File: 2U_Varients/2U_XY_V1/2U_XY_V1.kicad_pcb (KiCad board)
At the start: 4 copper layers, 83 x 212.6 mm, 31 parts, among them CN1 DF11-2DSA-4DP, J112 Conn_01x01, J114 Conn_01x01, J12 Conn_01x01, J14 Conn_01x01, J2 Conn_01x01, J3 Conn_01x01, J4 Conn_01x01, J5 Conn_01x01, U2 TMP112xxDRL, U3 DRV2605LDGS, U4 TCA4311ADGKR, U5 5040500691, U7 VEML6031X00

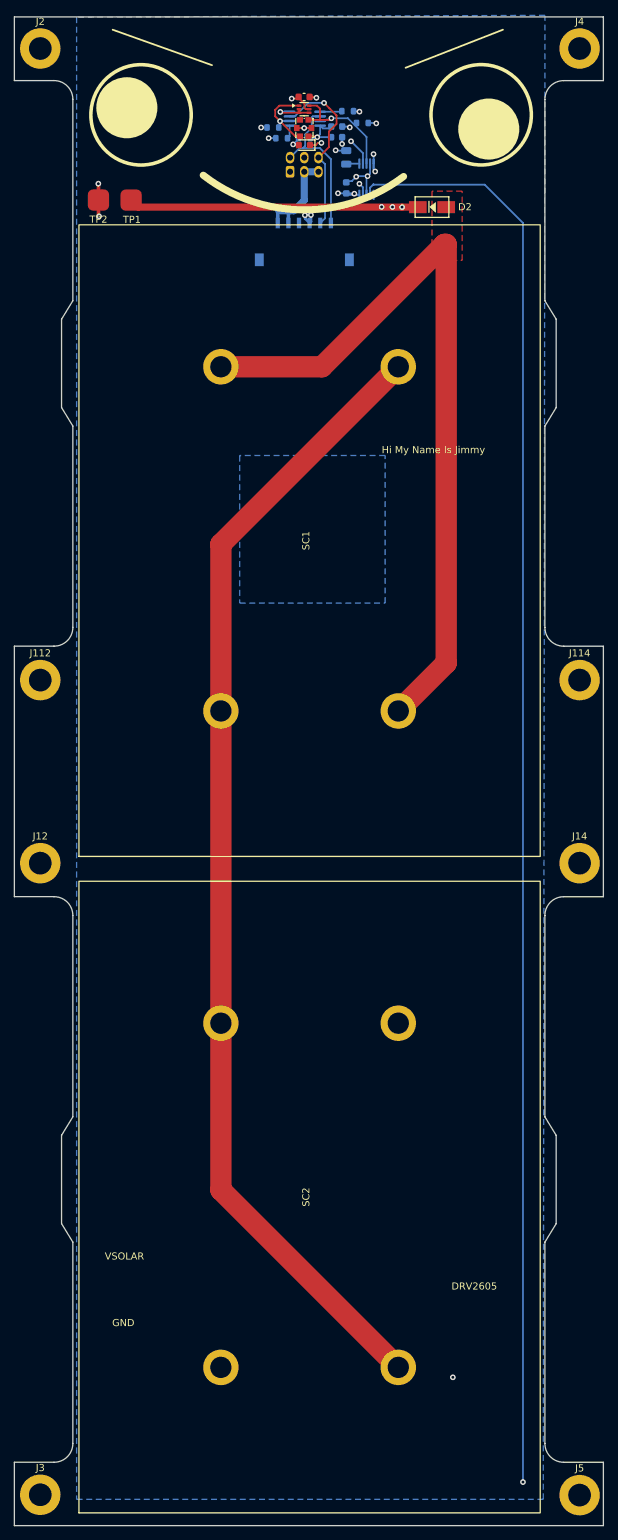
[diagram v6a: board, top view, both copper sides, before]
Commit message: Fixed Solar Cell Polarity
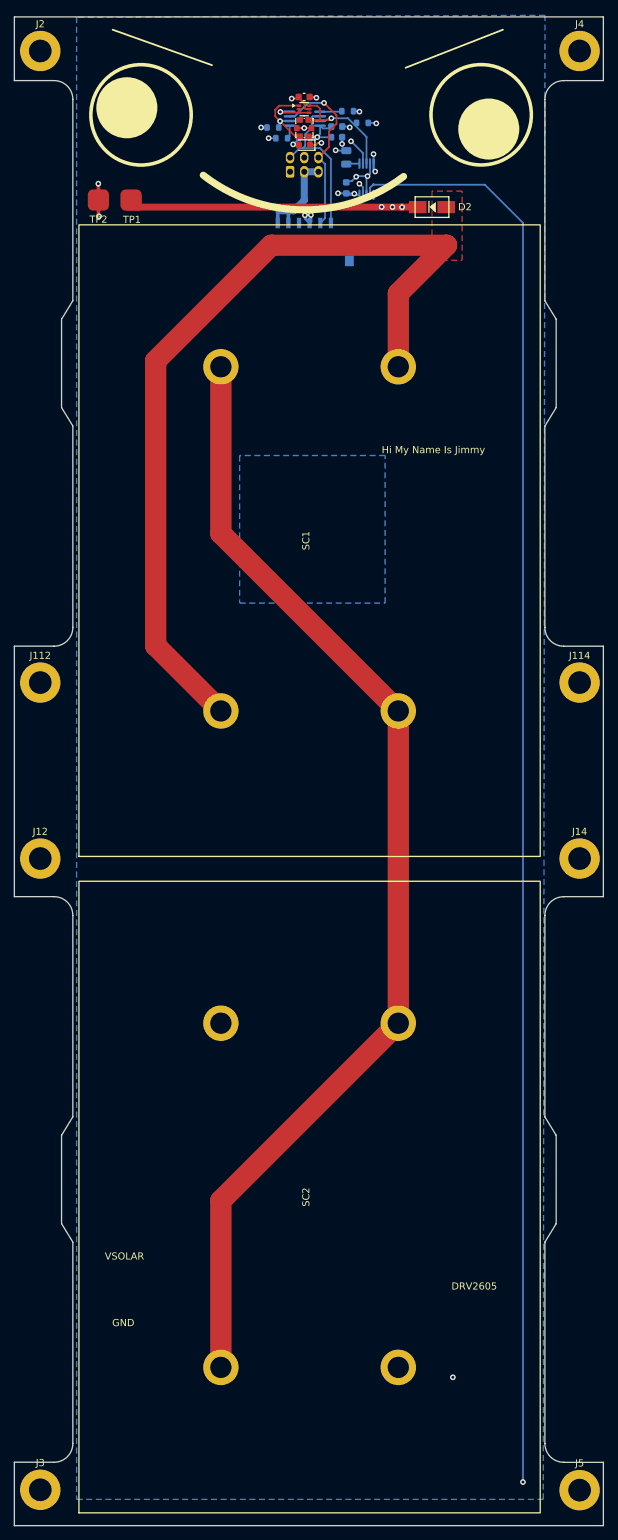
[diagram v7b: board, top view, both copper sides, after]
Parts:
- moved J3 0.70 mm to (171.8, 243.8)
- moved J5 0.70 mm to (247.8, 243.8)
- moved J12 0.65 mm to (171.8, 154.8)
- moved J14 0.65 mm to (247.8, 154.8)
- moved J2 0.35 mm to (171.8, 41.0)
- moved J4 0.35 mm to (247.8, 41.0)
- moved J112 0.35 mm to (171.8, 130.0)
- moved J114 0.35 mm to (247.8, 130.0)
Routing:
- net /SOL_OUT: track 107.4 -> 120.8 mm
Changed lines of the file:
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@@
 	(footprint "MountingHole:MountingHole_3.2mm_M3_ISO7380_Pad"
 		(layer "F.Cu")
-		(at 171.800001 40.65)
+		(at 171.800001 41)
 		(descr "Mounting Hole 3.2mm, M3, generated by kicad-footprint-generator mountinghole.py")
 		(tags "mountinghole M3 ISO7380")
@@
 	(footprint "MountingHole:MountingHole_3.2mm_M3_ISO7380_Pad"
 		(layer "F.Cu")
-		(at 247.800001 40.65)
+		(at 247.800001 41)
 		(descr "Mounting Hole 3.2mm, M3, generated by kicad-footprint-generator mountinghole.py")
 		(tags "mountinghole M3 ISO7380")
@@
 	(footprint "MountingHole:MountingHole_3.2mm_M3_ISO7380_Pad"
 		(layer "F.Cu")
-		(at 171.800001 244.45)
+		(at 171.800001 243.75)
 		(descr "Mounting Hole 3.2mm, M3, generated by kicad-footprint-generator mountinghole.py")
 		(tags "mountinghole M3 ISO7380")
@@
 			(layer "Dwgs.User")
 			(pts
-				(xy 177.25 85.5) (xy 197.25 85)
+				(xy 177.25 65.5) (xy 177.25 85.5)
 			)
-			(height 5.5)
-			(orientation 0)
+			(height -7)
+			(orientation 1)
 			(format
 				(prefix "")
@@
 			)
 			(gr_text "20"
-				(at 187.25 89.85 0)
+				(at 169.1 75.5 90)
 				(layer "Dwgs.User")
 				(effects
@@
 			(layer "Dwgs.User")
 			(pts
-				(xy 177.25 134.5) (xy 197.25 134.5)
+				(xy 177.25 154.5) (xy 177.25 134.5)
 			)
-			(height -4.5)
-			(orientation 0)
+			(height -2.5)
+			(orientation 1)
 			(format
 				(prefix "")
@@
 			)
 			(gr_text "20"
-				(at 187.25 128.85 0)
+				(at 173.6 144.5 90)
 				(layer "Dwgs.User")
 				(effects
@@
 			(layer "Dwgs.User")
 			(pts
-				(xy 177.25 65.5) (xy 177.25 85.5)
+				(xy 177.25 85.5) (xy 197.25 85)
 			)
-			(height -7)
-			(orientation 1)
+			(height 5.5)
+			(orientation 0)
 			(format
 				(prefix "")
@@
 			)
 			(gr_text "20"
-				(at 169.1 75.5 90)
+				(at 187.25 89.85 0)
 				(layer "Dwgs.User")
 				(effects
@@
 			(layer "Dwgs.User")
 			(pts
-				(xy 177.25 154.5) (xy 177.25 134.5)
+				(xy 242.25 65.5) (xy 222.25 65.5)
 			)
-			(height -2.5)
-			(orientation 1)
+			(height 97)
+			(orientation 0)
 			(format
 				(prefix "")
@@
 			)
 			(gr_text "20"
-				(at 173.6 144.5 90)
+				(at 232.25 161.35 0)
 				(layer "Dwgs.User")
 				(effects
@@
 			(layer "Dwgs.User")
 			(pts
-				(xy 242.25 65.5) (xy 222.25 65.5)
+				(xy 177.25 134.5) (xy 197.25 134.5)
 			)
-			(height 97)
+			(height -4.5)
 			(orientation 0)
 			(format
@@
 			)
 			(gr_text "20"
-				(at 232.25 161.35 0)
+				(at 187.25 128.85 0)
 				(layer "Dwgs.User")
 				(effects
@@
 		)
 		(pad "1" thru_hole circle
-			(at -48.5 0 90)
+			(at 0 0 90)
 			(size 5 5)
 			(drill 3)
@@
 		)
 		(pad "2" thru_hole circle
-			(at -48.5 -25 90)
+			(at 0 -25 90)
 			(size 5 5)
 			(drill 3)
@@
 		)
 		(pad "3" thru_hole circle
-			(at 0 -25 90)
+			(at -48.5 -25 90)
 			(size 5 5)
 			(drill 3)
@@
 		)
 		(pad "4" thru_hole circle
-			(at 0 0 90)
+			(at -48.5 0 90)
 			(size 5 5)
 			(drill 3)
@@
 	(footprint "MountingHole:MountingHole_3.2mm_M3_ISO7380_Pad"
 		(layer "F.Cu")
-		(at 247.800001 155.45)
+		(at 247.800001 154.8)
 		(descr "Mounting Hole 3.2mm, M3, generated by kicad-footprint-generator mountinghole.py")
 		(tags "mountinghole M3 ISO7380")
@@
 	(footprint "MountingHole:MountingHole_3.2mm_M3_ISO7380_Pad"
 		(layer "F.Cu")
-		(at 247.800001 129.65)
+		(at 247.800001 130)
 		(descr "Mounting Hole 3.2mm, M3, generated by kicad-footprint-generator mountinghole.py")
 		(tags "mountinghole M3 ISO7380")
@@
 	(footprint "MountingHole:MountingHole_3.2mm_M3_ISO7380_Pad"
 		(layer "F.Cu")
-		(at 247.8 244.5)
+		(at 247.8 243.8)
 		(descr "Mounting Hole 3.2mm, M3, generated by kicad-footprint-generator mountinghole.py")
 		(tags "mountinghole M3 ISO7380")
@@
 			(layer "Dwgs.User")
 			(pts
-				(xy 177.25 158) (xy 177.25 178)
+				(xy 177.25 178) (xy 197.25 177.5)
 			)
-			(height -7)
-			(orientation 1)
+			(height 5.5)
+			(orientation 0)
 			(format
 				(prefix "")
@@
 			)
 			(gr_text "20"
-				(at 169.1 168 90)
+				(at 187.25 182.35 0)
 				(layer "Dwgs.User")
 				(effects
@@
 			(layer "Dwgs.User")
 			(pts
-				(xy 242.25 158) (xy 222.25 158)
+				(xy 177.25 247) (xy 177.25 227)
 			)
-			(height 97)
-			(orientation 0)
+			(height -2.5)
+			(orientation 1)
 			(format
 				(prefix "")
@@
 			)
 			(gr_text "20"
-				(at 232.25 253.85 0)
+				(at 173.6 237 90)
 				(layer "Dwgs.User")
 				(effects
@@
 			(layer "Dwgs.User")
 			(pts
-				(xy 177.25 227) (xy 197.25 227)
+				(xy 177.25 158) (xy 177.25 178)
 			)
-			(height -4.5)
-			(orientation 0)
+			(height -7)
+			(orientation 1)
 			(format
 				(prefix "")
@@
 			)
 			(gr_text "20"
-				(at 187.25 221.35 0)
+				(at 169.1 168 90)
 				(layer "Dwgs.User")
 				(effects
@@
 			(layer "Dwgs.User")
 			(pts
-				(xy 177.25 178) (xy 197.25 177.5)
+				(xy 242.25 158) (xy 222.25 158)
 			)
-			(height 5.5)
+			(height 97)
 			(orientation 0)
 			(format
@@
 			)
 			(gr_text "20"
-				(at 187.25 182.35 0)
+				(at 232.25 253.85 0)
 				(layer "Dwgs.User")
 				(effects
@@
 			(layer "Dwgs.User")
 			(pts
-				(xy 177.25 247) (xy 177.25 227)
+				(xy 177.25 227) (xy 197.25 227)
 			)
-			(height -2.5)
-			(orientation 1)
+			(height -4.5)
+			(orientation 0)
 			(format
 				(prefix "")
@@
 			)
 			(gr_text "20"
-				(at 173.6 237 90)
+				(at 187.25 221.35 0)
 				(layer "Dwgs.User")
 				(effects
@@
 		)
 		(pad "1" thru_hole circle
-			(at -48.5 0 90)
+			(at 0 0 90)
 			(size 5 5)
 			(drill 3)
@@
 		)
 		(pad "2" thru_hole circle
-			(at -48.5 -25 90)
+			(at 0 -25 90)
 			(size 5 5)
 			(drill 3)
@@
 		)
 		(pad "3" thru_hole circle
-			(at 0 -25 90)
+			(at -48.5 -25 90)
 			(size 5 5)
 			(drill 3)
@@
 		)
 		(pad "4" thru_hole circle
-			(at 0 0 90)
+			(at -48.5 0 90)
 			(size 5 5)
 			(drill 3)
@@
 	(footprint "MountingHole:MountingHole_3.2mm_M3_ISO7380_Pad"
 		(layer "F.Cu")
-		(at 171.800001 155.45)
+		(at 171.800001 154.8)
 		(descr "Mounting Hole 3.2mm, M3, generated by kicad-footprint-generator mountinghole.py")
 		(tags "mountinghole M3 ISO7380")
@@
 	(footprint "MountingHole:MountingHole_3.2mm_M3_ISO7380_Pad"
 		(layer "F.Cu")
-		(at 171.800001 129.65)
+		(at 171.800001 130)
 		(descr "Mounting Hole 3.2mm, M3, generated by kicad-footprint-generator mountinghole.py")
 		(tags "mountinghole M3 ISO7380")
@@
 	)
 	(gr_text "-"
-		(at 225.66 187.48 0)
+		(at 201.3 186.5 0)
 		(layer "B.SilkS")
 		(effects
@@
 	)
 	(gr_text "-"
-		(at 201.25 142.96 0)
+		(at 225.7 142.7 0)
 		(layer "B.SilkS")
 		(effects
@@
 	)
 	(gr_text "+"
-		(at 225.83 142.86 0)
+		(at 200.8 142.8 0)
 		(layer "B.SilkS")
 		(effects
@@
 	)
 	(gr_text "-"
-		(at 225.95 94.42 0)
+		(at 201.75 93.15 0)
 		(layer "B.SilkS")
 		(effects
@@
 	)
 	(gr_text "+"
-		(at 200.58 187.86 0)
+		(at 225.3 187.6 0)
 		(layer "B.SilkS")
 		(effects
@@
 	)
 	(gr_text "+"
-		(at 225.88 235.71 0)
+		(at 201.3 235.4 0)
 		(layer "B.SilkS")
 		(effects
@@
 	)
 	(gr_text "-"
-		(at 201.25 237.46 0)
+		(at 225.65 235.05 0)
 		(layer "B.SilkS")
 		(effects
@@
 	)
 	(gr_text "+"
-		(at 200.78 94.33 0)
+		(at 226 93.7 0)
 		(layer "B.SilkS")
 		(effects
@@
 	)
 	(segment
-		(start 197.25 178)
-		(end 197.25 134)
+		(start 222.25 134)
+		(end 197.25 109)
 		(width 3)
 		(layer "F.Cu")
@@
 	)
 	(segment
-		(start 197.25 201.5)
-		(end 197.25 178)
+		(start 197.25 226.5)
+		(end 197.25 203)
 		(width 3)
 		(layer "F.Cu")
@@
 	)
 	(segment
-		(start 197.25 134)
-		(end 197.25 110.5)
+		(start 222.25 178)
+		(end 222.25 134)
 		(width 3)
 		(layer "F.Cu")
@@
 	)
 	(segment
-		(start 222.25 226.5)
-		(end 197.25 201.5)
+		(start 197.25 109)
+		(end 197.25 85.5)
 		(width 3)
 		(layer "F.Cu")
@@
 	)
 	(segment
-		(start 197.25 110.5)
-		(end 222.25 85.5)
+		(start 197.25 203)
+		(end 222.25 178)
 		(width 3)
 		(layer "F.Cu")
@@
 	)
 	(segment
-		(start 211.5 85.5)
-		(end 228.75 68.25)
+		(start 204.35 68.37)
+		(end 229.05 68.37)
 		(width 3)
 		(layer "F.Cu")
@@
 	)
 	(segment
-		(start 228.75 68.25)
-		(end 229 68.25)
+		(start 222.25 85.5)
+		(end 222.25 75.17)
 		(width 3)
 		(layer "F.Cu")
@@
 	)
 	(segment
-		(start 229 127.25)
-		(end 222.25 134)
+		(start 197.25 134)
+		(end 188.06 124.81)
+		(width 3)
+		(layer "F.Cu")
+		(net 22)
+	)
+	(segment
+		(start 188.06 124.81)
+		(end 188.06 84.66)
 		(width 3)
 		(layer "F.Cu")
@@
 	)
 	(segment
-		(start 229 68.25)
-		(end 229 127.25)
+		(start 222.25 75.17)
+		(end 229.05 68.37)
 		(width 3)
 		(layer "F.Cu")
@@
 	)
 	(segment
-		(start 197.25 85.5)
-		(end 211.5 85.5)
+		(start 188.06 84.66)
+		(end 204.35 68.37)
 		(width 3)
 		(layer "F.Cu")
